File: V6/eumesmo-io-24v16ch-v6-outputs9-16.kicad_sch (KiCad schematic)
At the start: 5 parts, among them Q12 MMBT2222A

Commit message: Renamed all files to eumesmo branding
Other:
- title: ESP 24V 16xIn/16xOut/1-Wire Module -> eumesmo 24V 16xIn/16xOut/1-Wire Module
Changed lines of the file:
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@@
 	(paper "A4")
 	(title_block
-		(title "ESP 24V 16xIn/16xOut/1-Wire Module")
-		(date "2026-02-10")
-		(rev "V6.1")
+		(title "eumesmo 24V 16xIn/16xOut/1-Wire Module")
+		(date "2026-06-13")
+		(rev "V6.2")
 	)
 	(text "RESISTORS: 62,5mW WHERE NOT SPECIFIED"
@@
 		)
 		(instances
-			(project "esp-24v-16ch-v6"
+			(project "eumesmo-io-24v16ch-v6"
 				(path "/2bc5a21a-1d79-419d-a592-6852cc07b00a/118d8d95-c0ce-4d84-8406-4e7809444f6f"
 					(reference "#PWR0242")
@@
 		)
 		(instances
-			(project "esp-24v-16ch-v6"
+			(project "eumesmo-io-24v16ch-v6"
 				(path "/2bc5a21a-1d79-419d-a592-6852cc07b00a/118d8d95-c0ce-4d84-8406-4e7809444f6f"
 					(reference "Q13")
@@
 		)
 		(instances
-			(project "esp-24v-16ch-v6"
+			(project "eumesmo-io-24v16ch-v6"
 				(path "/2bc5a21a-1d79-419d-a592-6852cc07b00a/118d8d95-c0ce-4d84-8406-4e7809444f6f"
 					(reference "#PWR0244")
@@
 		)
 		(instances
-			(project "esp-24v-16ch-v6"
+			(project "eumesmo-io-24v16ch-v6"
 				(path "/2bc5a21a-1d79-419d-a592-6852cc07b00a/118d8d95-c0ce-4d84-8406-4e7809444f6f"
 					(reference "R117")
@@
 		)
 		(instances
-			(project "esp-24v-16ch-v6"
+			(project "eumesmo-io-24v16ch-v6"
 				(path "/2bc5a21a-1d79-419d-a592-6852cc07b00a/118d8d95-c0ce-4d84-8406-4e7809444f6f"
 					(reference "#PWR0243")
@@
 		)
 		(instances
-			(project "esp-24v-16ch-v6"
+			(project "eumesmo-io-24v16ch-v6"
 				(path "/2bc5a21a-1d79-419d-a592-6852cc07b00a/118d8d95-c0ce-4d84-8406-4e7809444f6f"
 					(reference "R118")
@@
 		)
 		(instances
-			(project "esp-24v-16ch-v6"
+			(project "eumesmo-io-24v16ch-v6"
 				(path "/2bc5a21a-1d79-419d-a592-6852cc07b00a/118d8d95-c0ce-4d84-8406-4e7809444f6f"
 					(reference "D67")
@@
 		)
 		(instances
-			(project "esp-24v-16ch-v6"
+			(project "eumesmo-io-24v16ch-v6"
 				(path "/2bc5a21a-1d79-419d-a592-6852cc07b00a/118d8d95-c0ce-4d84-8406-4e7809444f6f"
 					(reference "R116")

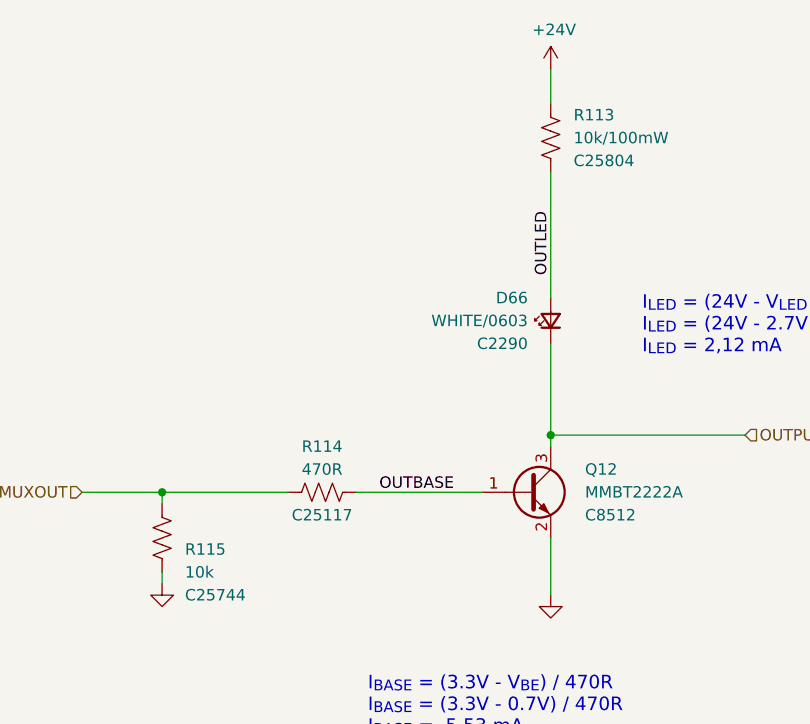
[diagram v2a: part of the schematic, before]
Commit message: Added CPU health LED
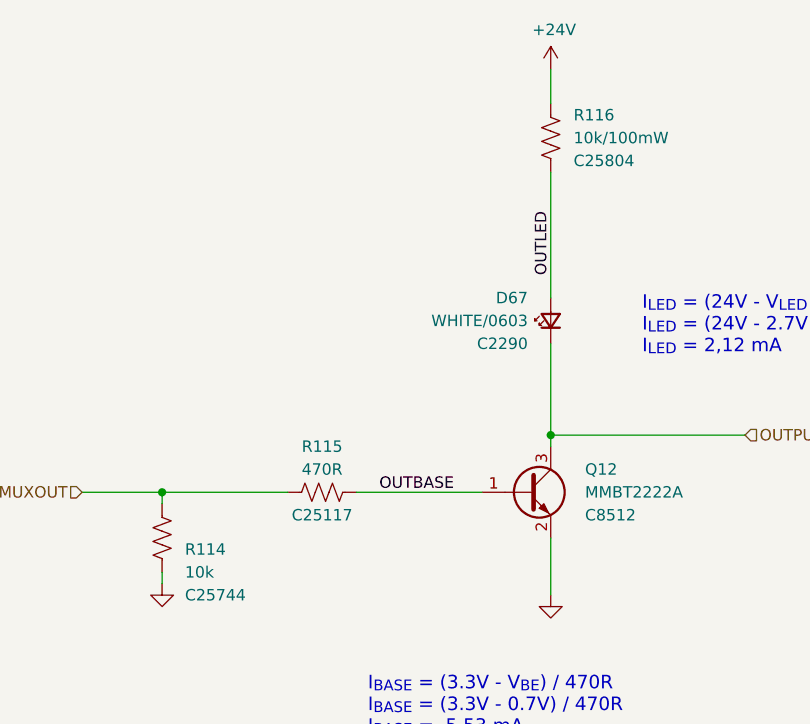
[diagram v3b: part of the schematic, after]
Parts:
- renumbered D66 to D67, R115 to R114, R114 to R115, R113 to R116
